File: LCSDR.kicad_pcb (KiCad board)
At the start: 2 copper layers, 150 x 95 mm, 158 parts, among them J1 Conn_01x10, J10 Conn_01x01, J11 Conn_01x01, J2 Conn_01x10, J3 phones, J4 MIC_PTT, J5 Conn_01x10, J8 Conn_01x01, J9 Conn_01x01, K1 FRT5, Q1 2N7002, Q2 BC847, T1 Transformer_1P_2S, T2 Transformer_1P_2S, U1 74LVC1G74, U10 NE5532, U11 MC33079, U12 NC7SB3157, U13 NC7SB3157, U14 NC7SB3157, U15 NC7SB3157, U2 74LVC74APW, U3 74LVC74APW, U4 74LVC1G74, U6 NE5532, U8 4053, U9 4053

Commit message: first edit
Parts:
- removed C21: 22..47nF, UI:C_1206_0603
- removed C39, C70: 10uF, Capacitors_THT:CP_Radial_D5.0mm_P2.00mm
- removed C42, C69: 100nF, UI:C_1206_0603
- removed C52, C53, C54, C55: 1uF, Capacitors_THT:CP_Radial_D5.0mm_P2.00mm
- removed C71, C72, C73, C74: 2.2nF, UI:C_1206_0603
- removed C77, C78, C79, C80: 10uF, Capacitors_Tantalum_SMD:CP_Tantalum_Case-A_EIA-3216-18_Wave
- removed R17, R22, R23, R5, R6: 10k, UI:R_1206_0603
- removed R61, R64, R65: 1k, UI:R_1206_0603
- removed R62, R63: 91, UI:R_1206_0603
- removed T1, T2: Transformer_1P_2S, UI:HF1_9
- removed U12, U13, U14, U15: NC7SB3157, TO_SOT_Packages_SMD:SOT-23-6
- removed U4: 74LVC1G74, Housings_SSOP:TSSOP-8_3x3mm_Pitch0.65mm
- removed U8, U9: 4053, Housings_SOIC:SOIC-16_3.9x9.9mm_Pitch1.27mm
- added C25: 10uF, Capacitors_Tantalum_SMD:CP_Tantalum_Case-A_EIA-3216-18_Wave, F.Cu at (140.0, 145.1)
- added K2, K3: FRT5, Relays_THT:Relay_DPDT_FRT5, F.Cu at (140.0, 145.1)
- added L2: 47uH, Choke_Axial_ThroughHole:Choke_Horizontal_RM10mm, F.Cu at (140.0, 145.1)
- added R10, R9: 1k, UI:R_1206_0603, F.Cu at (140.0, 145.1)
- added R3, R4, R7: 30, UI:R_1206_0603, F.Cu at (140.0, 145.1)
- added R8: 1k, Resistors_SMD:R_0603_HandSoldering, F.Cu at (140.0, 145.1)
- added U5: FST3253, Housings_SSOP:TSSOP-16_4.4x5mm_Pitch0.65mm, F.Cu at (140.0, 145.1)
- C1, C2, C44, C47, C59, C60, C61, C63, C64, C66, C67, C68: footprint UI:C_1206_0603 -> Capacitors_SMD:C_0603_HandSoldering
- C3, C45, C58: footprint Capacitors_THT:CP_Radial_D5.0mm_P2.00mm -> Capacitors_Tantalum_SMD:CP_Tantalum_Case-A_EIA-3216-18_Wave
- C5: value 10uF -> 100nF; footprint Capacitors_THT:CP_Radial_D5.0mm_P2.00mm -> UI:C_1206_0603; moved to F.Cu
- C6: value 100nF -> 22uF; footprint UI:C_1206_0603 -> Capacitors_Tantalum_SMD:CP_Tantalum_Case-A_EIA-3216-18_Wave
- C62, C65: footprint Capacitors_THT:CP_Radial_D5.0mm_P2.00mm -> Capacitors_Tantalum_SMD:CP_Tantalum_Case-A_EIA-3216-18_Wave; moved to F.Cu
- C7: value 10uF -> 100nF; footprint Capacitors_THT:CP_Radial_D5.0mm_P2.00mm -> Capacitors_SMD:C_0603_HandSoldering; moved to F.Cu
- C76: value 10uF -> 22uF; footprint Capacitors_THT:CP_Radial_D5.0mm_P2.00mm -> Capacitors_Tantalum_SMD:CP_Tantalum_Case-A_EIA-3216-18_Wave
- L1: footprint Resistors_THT:R_Axial_DIN0207_L6.3mm_D2.5mm_P10.16mm_Horizontal -> Choke_Axial_ThroughHole:Choke_Horizontal_RM10mm
- R1, R2, R37, R38, R39, R40, R41, R42, R43, R44, R45, R46, R47, R48, R49, R50, R51, R52, R53, R54, R55, R56, R57, R58, R59, R60: footprint UI:R_1206_0603 -> Resistors_SMD:R_0603_HandSoldering
- R66: value 91 -> 30
- R67: value 91 -> 1k
- R68: value 1k -> 10R
- U1: value 74LVC1G74 -> 4053; footprint Housings_SSOP:TSSOP-8_3x3mm_Pitch0.65mm -> Housings_SSOP:TSSOP-16_4.4x5mm_Pitch0.65mm
- U3: value 74LVC74APW -> 4053; footprint Housings_SSOP:TSSOP-14_4.4x5mm_Pitch0.65mm -> Housings_SSOP:TSSOP-16_4.4x5mm_Pitch0.65mm
- moved U3 50.4 mm to (140.0, 145.1), turned to 0 degrees
- moved C6 49.7 mm to (140.0, 145.1), turned to 0 degrees
- moved C7 47.1 mm to (140.0, 145.1), turned to 0 degrees
- moved C4 40.2 mm to (140.0, 145.1), turned to 0 degrees
- moved C5 39.8 mm to (140.0, 145.1), turned to 0 degrees
- moved R2 32.9 mm to (140.0, 145.1)
- moved U1 31.4 mm to (182.3, 105.7)
- moved C65 0.34 mm to (165.8, 98.3)
- moved C62 0.19 mm to (165.7, 91.1)
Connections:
- net /switching/L renamed /s2/L
- net /switching/R renamed /s2/R
- net RX_P90 renamed Net-(U2-Pad2)
- C4 pad 1: Net-(C4-Pad1) -> GND
- C4 pad 2: GND -> Net-(C4-Pad2)
- C43 pad 1: +9V -> Net-(C43-Pad1)
- C48 pad 1: Net-(C21-Pad1) -> Net-(C43-Pad1)
- C5 pad 1: Net-(C4-Pad1) -> (no net)
- C5 pad 2: GND -> Net-(C5-Pad2)
- C6 pad 1: Net-(C6-Pad1) -> Net-(C4-Pad2)
- C7 pad 1: Net-(C6-Pad1) -> VDD
- C85 pad 1: RX_180 -> M_180
- C86 pad 1: RX_0 -> M_0
- C87 pad 1: RX_270 -> M_270
- C88 pad 1: RX_90 -> M_90
- J2 pad 1: (no net) -> Voltage1
- J2 pad 2: ~RX -> (no net)
- J2 pad 3: ~TX -> (no net)
- K1 pad 2: Net-(K1-Pad2) -> (no net)
- K1 pad 7: Net-(K1-Pad2) -> (no net)
- L1 pad 1: (no net) -> Voltage1
- Q1 pad 3: Net-(C21-Pad1) -> Net-(C43-Pad1)
- R2 pad 1: Net-(C1-Pad1) -> CLK
- R26 pad 1: +9V -> (no net)
- R66 pad 2: Net-(R66-Pad2) -> Net-(C81-Pad1)
- R67 pad 1: Net-(R67-Pad1) -> Net-(C5-Pad2)
- R67 pad 2: Net-(R67-Pad2) -> Net-(C4-Pad2)
- R68 pad 1: Net-(C75-Pad2) -> Net-(C5-Pad2)
- R68 pad 2: Net-(C4-Pad1) -> Net-(R68-Pad2)
- U1 pad 1: Net-(C1-Pad1) -> RX_270
- U1 pad 2: /PhaseRotators/RX180 -> TX_270
- U1 pad 3: /PhaseRotators/RX180 -> RX_0
- U1 pad 4: GND -> M_0
- U1 pad 5: /PhaseRotators/RX0 -> TX_0
- U1 pad 6: ~RX -> GND
- U1 pad 7: VCC -> GND
- U1 pad 8: VCC -> GND
- U2 pad 11: /PhaseRotators/RX0 -> Net-(C1-Pad1)
- U2 pad 3: /PhaseRotators/RX180 -> Net-(C1-Pad1)
- U2 pad 5: RX_P0 -> P90
- U2 pad 6: (no net) -> Net-(U2-Pad12)
- U2 pad 8: Net-(U2-Pad12) -> P0
- U3 pad 1: VCC -> RX_180
- U3 pad 10: VCC -> Net-(U1-Pad10)
- U3 pad 11: /PhaseRotators/TX0 -> Net-(U1-Pad10)
- U3 pad 12: Net-(U3-Pad12) -> (no net)
- U3 pad 13: VCC -> (no net)
- U3 pad 14: VCC -> (no net)
- U3 pad 2: TX_P90 -> TX_180
- U3 pad 3: /PhaseRotators/TX180 -> RX_90
- U3 pad 4: VCC -> M_90
- U3 pad 5: TX_P0 -> TX_90
- U3 pad 6: (no net) -> GND
- U3 pad 8: Net-(U3-Pad12) -> GND
- U3 pad 9: TX_P90 -> Net-(U1-Pad10)
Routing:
- net (no net): track 0.00 -> 68.8 mm, vias 0 -> 4
- net VCC: track 24.5 -> 0.00 mm
- net TX_P90: track 16.1 -> 0.00 mm, vias 2 -> 0
- net TX_P0: track 10.1 -> 0.00 mm
- net Net-(U3-Pad12): track 7.90 -> 0.00 mm
- net Net-(C74-Pad1): track 5.88 -> 0.00 mm
- net Net-(C71-Pad1): track 5.88 -> 0.00 mm
- net Net-(C72-Pad1): track 5.86 -> 0.00 mm
- net Net-(U1-Pad10): track 0.00 -> 5.86 mm
- net Net-(C73-Pad1): track 5.86 -> 0.00 mm
- net GND: track 9.04 -> 6.14 mm, vias 4 -> 2
- net /PhaseRotators/TX180: track 2.89 -> 0.00 mm, vias 1 -> 0
- net Net-(C56-Pad1): track 2.60 -> 0.00 mm

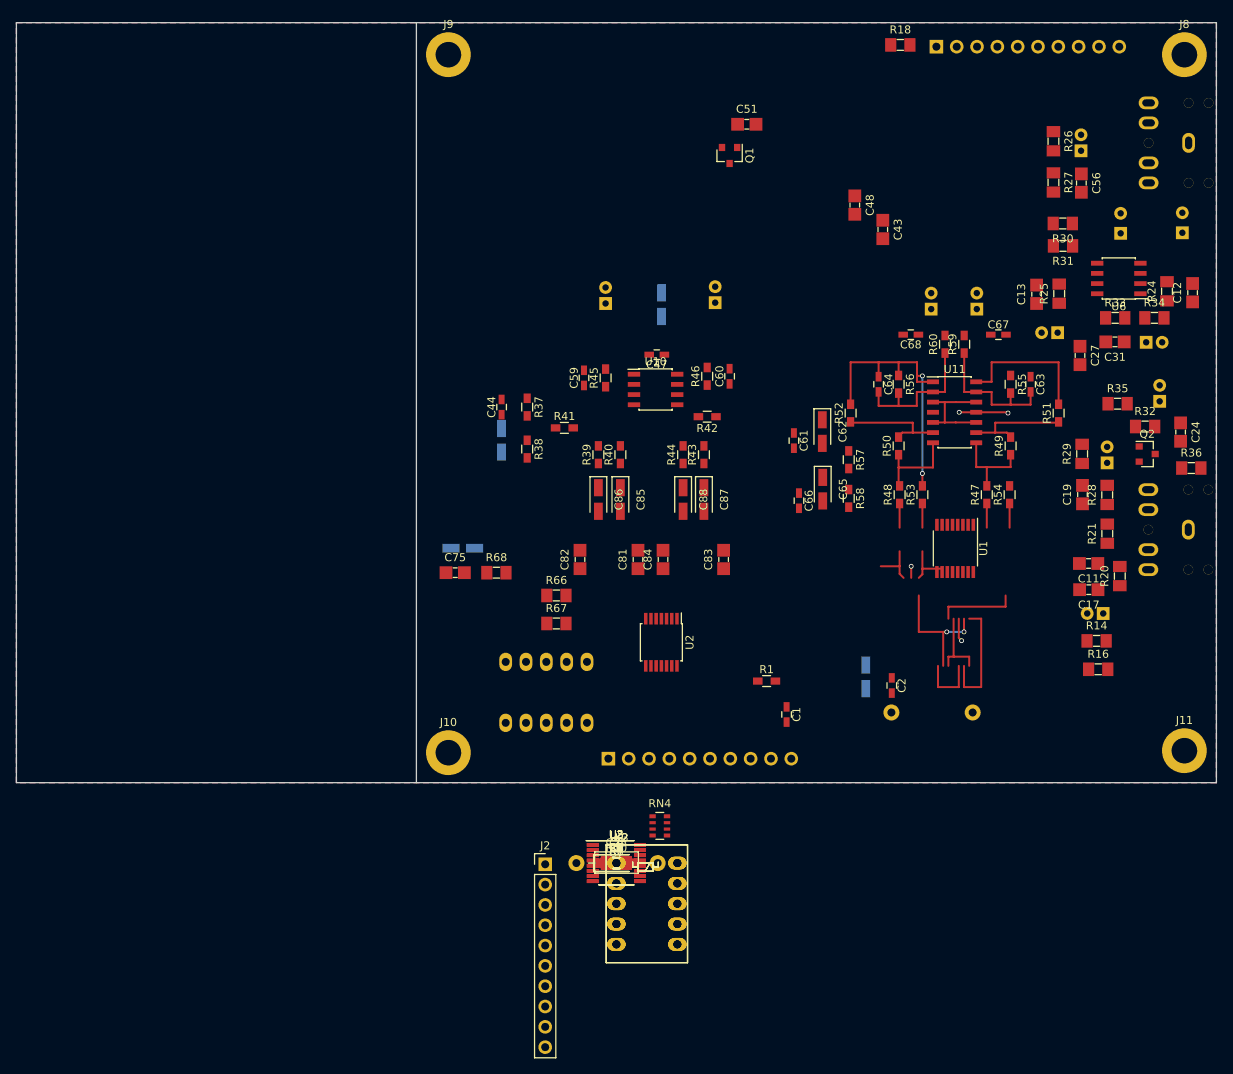
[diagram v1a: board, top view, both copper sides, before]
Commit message: rotators 2 74lvc1G74
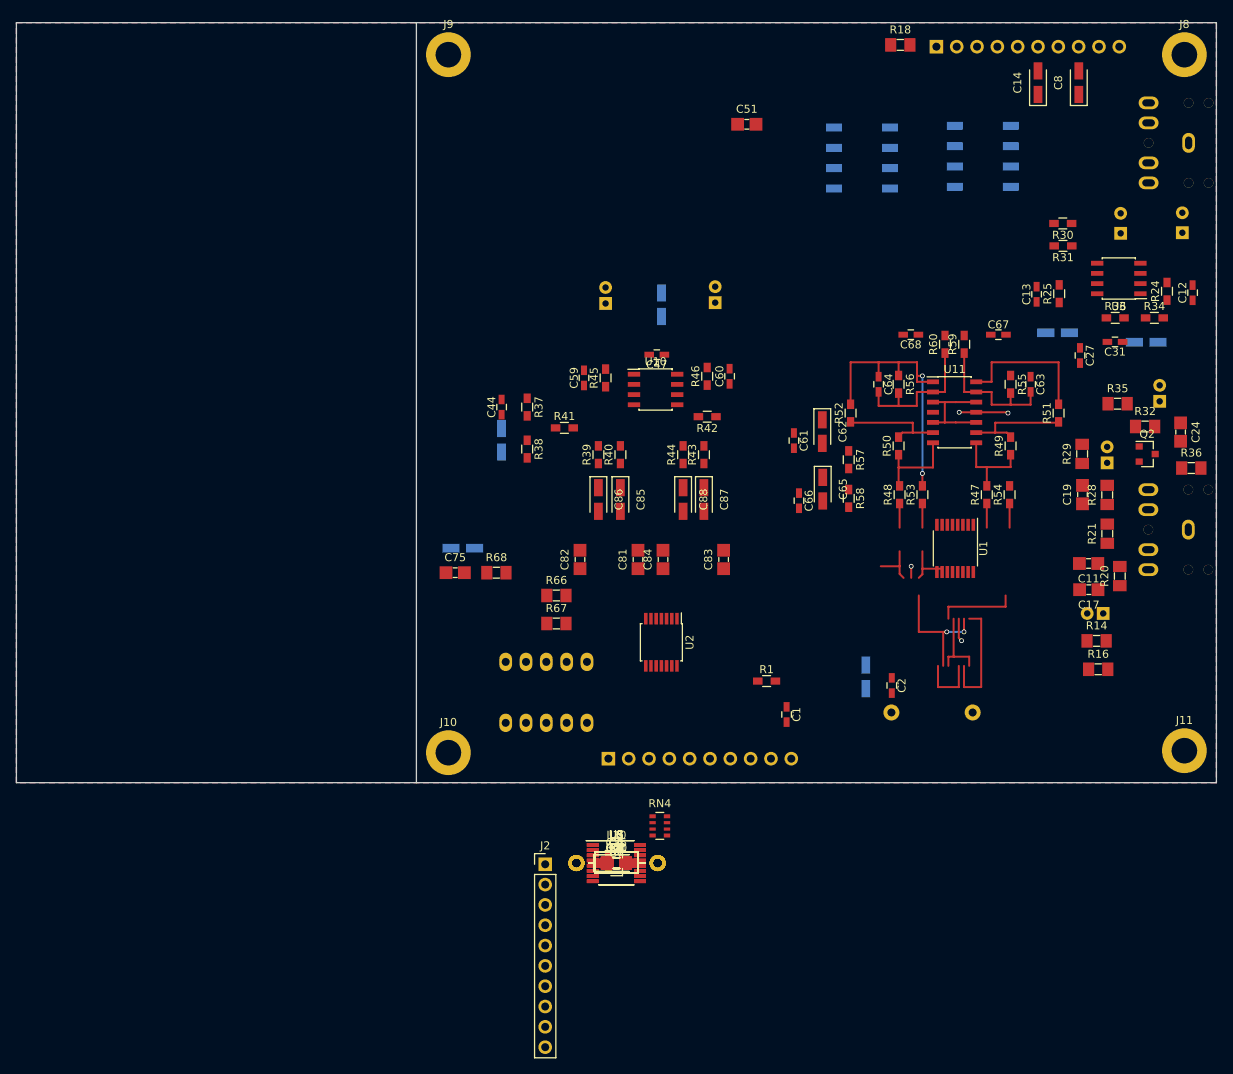
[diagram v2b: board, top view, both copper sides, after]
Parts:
- removed C43, C56: 100nF, UI:C_1206_0603
- removed C48: 22..47nF, UI:C_1206_0603
- removed C57: 10uF, Capacitors_THT:CP_Radial_D5.0mm_P2.00mm
- removed R26, R27: 10k, UI:R_1206_0603
- added C21: 100nF, UI:C_1206_0603, F.Cu at (140.0, 145.1)
- added L10: 33uH, Choke_Axial_ThroughHole:Choke_Horizontal_RM10mm, F.Cu at (140.0, 145.1)
- added L5: 22uH, Choke_Axial_ThroughHole:Choke_Horizontal_RM10mm, F.Cu at (140.0, 145.1)
- added L6: 100uH, Choke_Axial_ThroughHole:Choke_Horizontal_RM10mm, F.Cu at (140.0, 145.1)
- C12, C13, C27, C31: footprint UI:C_1206_0603 -> Capacitors_SMD:C_0603_HandSoldering
- C14, C8: value 1uF -> 4.7uF; footprint Capacitors_THT:CP_Radial_D5.0mm_P2.00mm -> Capacitors_Tantalum_SMD:CP_Tantalum_Case-A_EIA-3216-18_Wave; moved to F.Cu
- C22, C23: footprint Capacitors_THT:CP_Radial_D5.0mm_P2.00mm -> Capacitors_Tantalum_SMD:CP_Tantalum_Case-A_EIA-3216-18_Wave
- K2, K3: value FRT5 -> G6K-2F; footprint Relays_THT:Relay_DPDT_FRT5 -> UI:Relay_G6K-2F; moved to B.Cu
- Q1: value 2N7002 -> MMBT2222LT1G
- R24, R25, R30, R31, R33, R34: footprint UI:R_1206_0603 -> Resistors_SMD:R_0603_HandSoldering
- moved K3 104.5 mm to (189.3, 52.9), turned to 180 degrees
- moved K2 98.1 mm to (174.2, 53.1), turned to 180 degrees
- moved Q1 89.6 mm to (140.0, 145.1), turned to 0 degrees
- moved C8 33.8 mm to (197.8, 47.5)
- moved C14 29.3 mm to (192.7, 47.5)
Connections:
- C14 pad 1: Q_OUT -> Net-(C14-Pad1)
- C14 pad 2: Net-(C14-Pad2) -> LINE_OUT_LEFT
- C8 pad 1: I_OUT -> Net-(C8-Pad1)
- C8 pad 2: Net-(C8-Pad2) -> LINE_OUT_RIGHT
- K2 pad 10: Net-(C43-Pad1) -> (no net)
- K3 pad 10: (no net) -> Net-(C21-Pad1)
- K3 pad 2: Net-(C14-Pad2) -> Net-(K3-Pad2)
- K3 pad 3: LINE_OUT_LEFT -> Net-(C14-Pad1)
- K3 pad 4: Net-(K3-Pad4) -> Q_OUT
- K3 pad 7: Net-(K3-Pad7) -> I_OUT
- K3 pad 8: LINE_OUT_RIGHT -> Net-(C8-Pad1)
- K3 pad 9: Net-(C8-Pad2) -> Net-(K3-Pad9)
- Q1 pad 3: Net-(C43-Pad1) -> Net-(C21-Pad1)
- R30 pad 2: Net-(K3-Pad4) -> Net-(K3-Pad2)
- R31 pad 2: Net-(K3-Pad7) -> Net-(K3-Pad9)

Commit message: PCB s1
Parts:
- removed K1: FRT5, Relays_THT:Relay_DPDT_FRT5
- added L7: 22uH, Choke_Axial_ThroughHole:Choke_Horizontal_RM10mm, F.Cu at (140.0, 145.1)
- added L8: 22uH, Choke_Axial_ThroughHole:Choke_Horizontal_RM10mm, B.Cu at (181.4, 80.8)
- added U4: 74LVC1G74, Housings_SSOP:TSSOP-8_4.4x3mm_Pitch0.65mm, F.Cu at (164.7, 118.8)
- added U7: FSA3157, TO_SOT_Packages_SMD:SOT-363_SC-70-6, F.Cu at (164.9, 108.5)
- C15, C16: footprint Capacitors_THT:CP_Radial_D5.0mm_P2.00mm -> Capacitors_Tantalum_SMD:CP_Tantalum_Case-A_EIA-3216-18_Wave; moved to F.Cu
- C22, C58: moved to F.Cu
- C81, C82, C83, C84: moved to B.Cu
- U2: value 74LVC74APW -> 74LVC1G74; footprint Housings_SSOP:TSSOP-14_4.4x5mm_Pitch0.65mm -> Housings_SSOP:TSSOP-8_4.4x3mm_Pitch0.65mm
- U5: value FST3253 -> FSA3157; footprint Housings_SSOP:TSSOP-16_4.4x5mm_Pitch0.65mm -> TO_SOT_Packages_SMD:SOT-363_SC-70-6
- moved U3 56.5 mm to (149.8, 89.4), turned to 180 degrees
- moved R7 47.6 mm to (163.5, 103.7), turned to 90 degrees
- moved R3 46.1 mm to (160.4, 103.7), turned to 90 degrees
- moved R4 44.8 mm to (157.2, 103.7), turned to 90 degrees
- moved U5 41.1 mm to (159.0, 108.6), turned to 270 degrees
- moved C66 36.9 mm to (187.3, 72.2), turned to 90 degrees
- moved R66 35.0 mm to (166.6, 103.7), turned to 90 degrees
- moved C65 30.0 mm to (187.3, 77.4)
- moved R41 29.5 mm to (145.8, 63.8), turned to 270 degrees
- moved R58 27.9 mm to (184.8, 76.5)
- moved R57 27.4 mm to (184.8, 72.2)
- moved R42 26.6 mm to (143.8, 63.8), turned to 270 degrees
- moved C85 26.2 mm to (166.6, 97.1)
- moved C81 25.9 mm to (166.6, 97.1)
- moved R54 24.0 mm to (174.3, 80.2)
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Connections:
- C85 pad 1: M_180 -> M_90
- C86 pad 1: M_0 -> M_180
- C87 pad 1: M_270 -> M_0
- C88 pad 1: M_90 -> M_270
- U1 pad 1: RX_270 -> (no net)
- U1 pad 12: (no net) -> TX_270
- U1 pad 13: (no net) -> RX_270
- U1 pad 14: (no net) -> M_270
- U1 pad 15: M_270 -> (no net)
- U1 pad 2: TX_270 -> (no net)
- U1 pad 3: RX_0 -> RX_90
- U1 pad 4: M_0 -> M_90
- U1 pad 5: TX_0 -> TX_90
- U2 pad 1: VCC -> Net-(C1-Pad1)
- U2 pad 3: Net-(C1-Pad1) -> Net-(U2-Pad3)
- U2 pad 4: VCC -> GND
- U2 pad 6: Net-(U2-Pad12) -> VCC
- U2 pad 7: GND -> VCC
- U2 pad 8: P0 -> VCC
- U3 pad 1: RX_180 -> (no net)
- U3 pad 12: (no net) -> TX_180
- U3 pad 13: (no net) -> RX_180
- U3 pad 14: (no net) -> M_180
- U3 pad 15: M_180 -> (no net)
- U3 pad 2: TX_180 -> (no net)
- U3 pad 3: RX_90 -> RX_0
- U3 pad 4: M_90 -> M_0
- U3 pad 5: TX_90 -> TX_0
- U5 pad 1: GND -> Net-(R3-Pad1)
- U5 pad 2: P90 -> GND
- U5 pad 3: Net-(R7-Pad1) -> Net-(R4-Pad1)
- U5 pad 4: Net-(R4-Pad1) -> Net-(R68-Pad2)
- U5 pad 5: Net-(R66-Pad1) -> Net-(C75-Pad2)
- U5 pad 6: Net-(R3-Pad1) -> P0
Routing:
- net (no net): track 68.8 -> 0.00 mm, vias 4 -> 0
- net RX_90: track 0.00 -> 45.5 mm, vias 0 -> 2
- net Net-(C64-Pad1): track 35.4 -> 0.00 mm, vias 2 -> 0
- net RX_270: track 0.00 -> 29.8 mm, vias 0 -> 2
- net TX_0: track 2.92 -> 27.0 mm, vias 0 -> 2
- net RX_0: track 0.00 -> 16.0 mm
- net Net-(R42-Pad2): track 0.00 -> 15.9 mm
- net Net-(R39-Pad2): track 0.00 -> 15.9 mm
- net M_180: track 0.00 -> 15.7 mm
- net Net-(R49-Pad2): track 13.7 -> 0.00 mm
- net M_0: track 0.00 -> 13.6 mm
- net M_90: track 0.00 -> 13.5 mm
- net Net-(R50-Pad2): track 13.5 -> 0.00 mm
- net Net-(C63-Pad1): track 17.9 -> 4.76 mm
- net Net-(C60-Pad1): track 0.00 -> 11.6 mm
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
